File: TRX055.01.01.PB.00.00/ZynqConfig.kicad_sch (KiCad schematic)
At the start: 1 part, among them U1 XC7Z015-1CLG485I

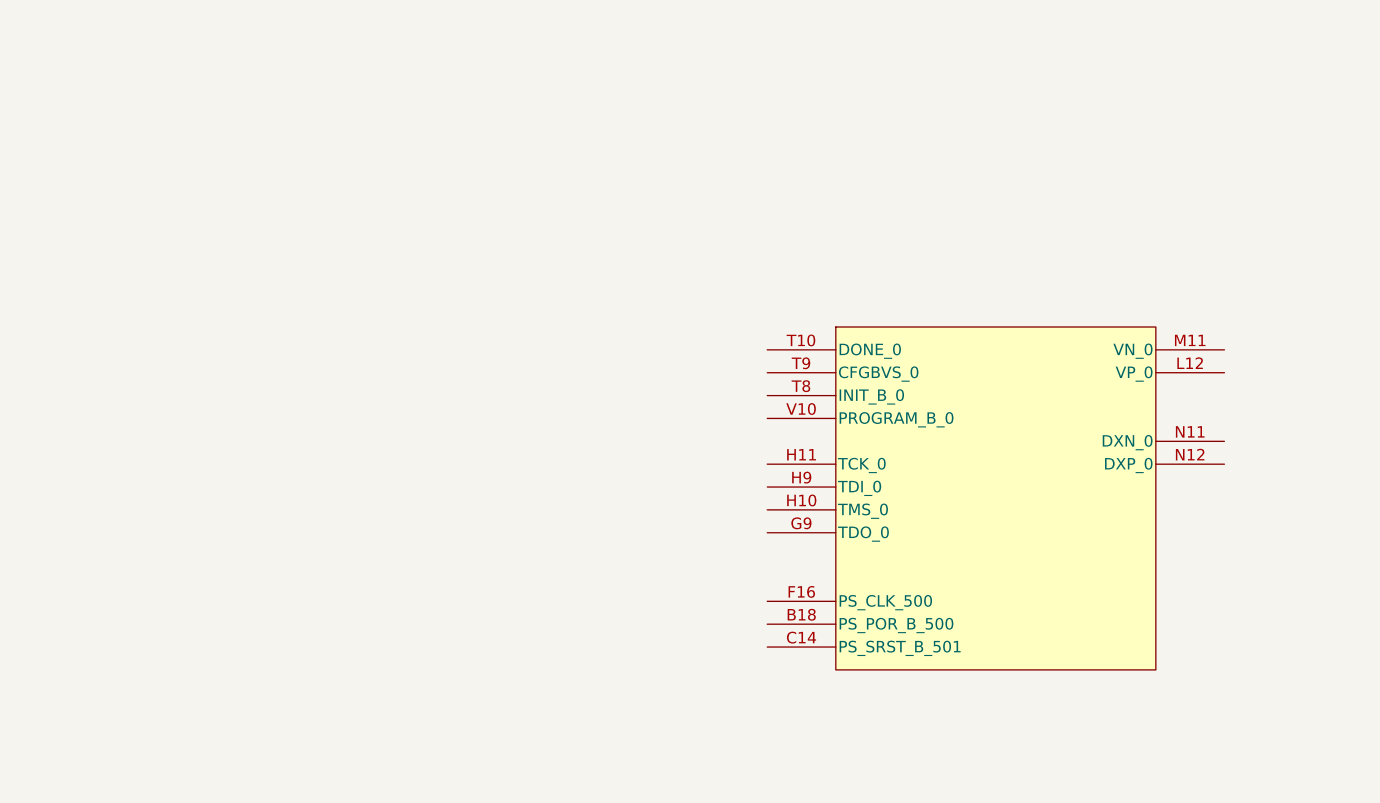
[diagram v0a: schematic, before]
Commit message: + add clocks + add PSU
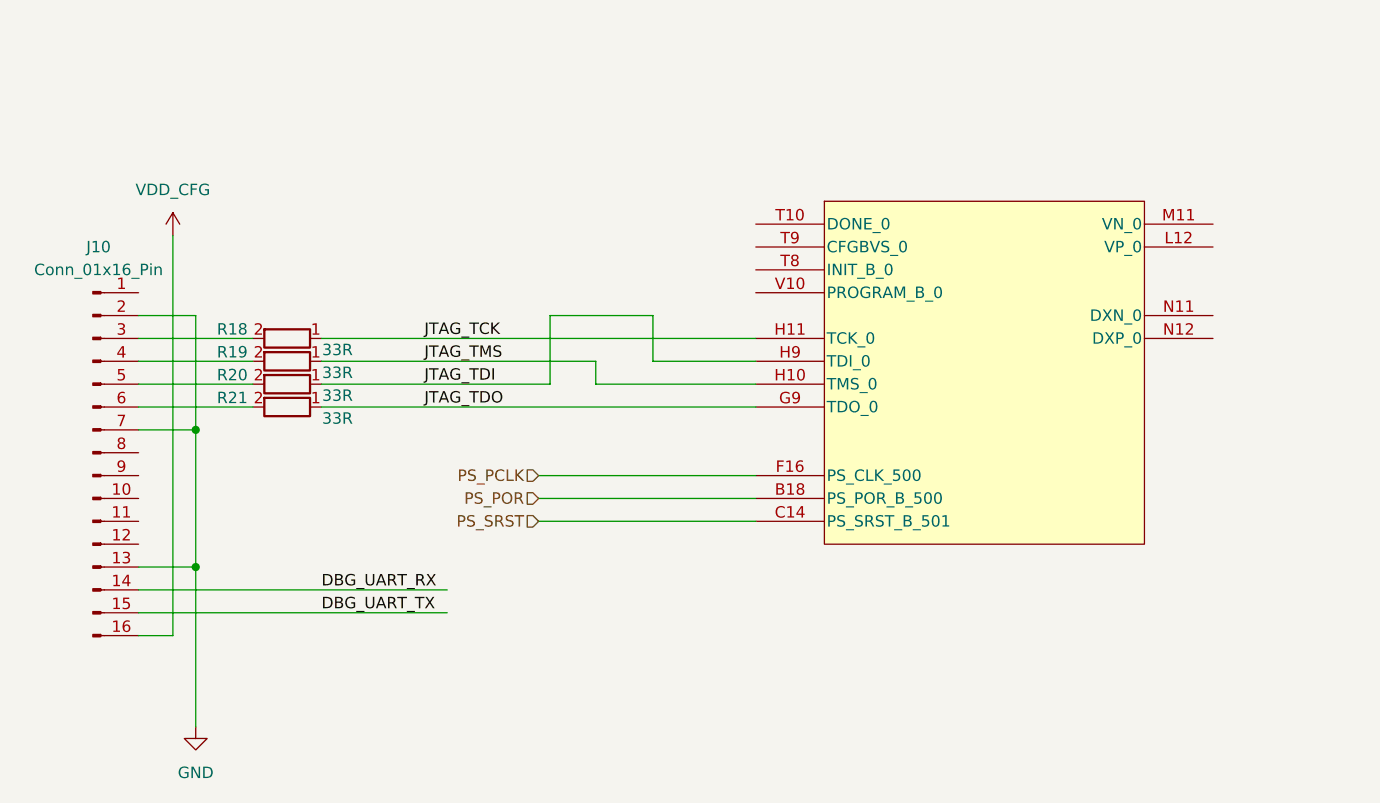
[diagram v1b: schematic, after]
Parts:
- added J10: Conn_01x16_Pin, foot-ppa-passive:FH34SRJ-16S-0.5SH, symbol Connector:Conn_01x16_Pin
- added R18, R19, R20, R21: 33R, Resistor_SMD:R_0402_1005Metric, symbol PPA-Pasive:Res
- U1: value XC7Z015-1CLG485I -> XC7Z015-2CLG485I; JLCPCB Part # C1522056 -> C1522056
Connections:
- net PS_POR: now reaches U1.B18 (PS_POR_B_500)
- net PS_SRST: now reaches U1.C14 (PS_SRST_B_501)
- net PS_PCLK: now reaches U1.F16 (PS_CLK_500)
- net JTAG_TDO: now reaches U1.G9 (TDO_0)
- net JTAG_TDO: now also R21.1
- net JTAG_TMS: now reaches U1.H10 (TMS_0)
- net JTAG_TMS: now also R19.1
- net JTAG_TCK: now reaches U1.H11 (TCK_0)
- net JTAG_TCK: now also R18.1
- net JTAG_TDI: now reaches U1.H9 (TDI_0)
- net JTAG_TDI: now also R20.1
- new net: J10.3 (Pin_3), R18.2
- new net: J10.4 (Pin_4), R19.2
- new net: J10.6 (Pin_6), R21.2
- new net: J10.5 (Pin_5), R20.2
- new net DBG_UART_RX: J10.14 (Pin_14)
- new net DBG_UART_TX: J10.15 (Pin_15)
- new net GND: J10.13 (Pin_13), J10.2 (Pin_2), J10.7 (Pin_7)
- new net VDD_CFG: J10.16 (Pin_16)

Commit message: V0.1 - production, added brig-up comments
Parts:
- added R155, R156, R159: 10K, Resistor_SMD:R_0402_1005Metric, symbol PPA-Pasive:Res
- U1: footprint CLG485XC7Z012S/XC7Z015_AMD -> XC7Z015:CLG485XC7Z012S&slash_XC7Z015_AMD
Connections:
- net GND: now also U1.T9 (CFGBVS_0), R159.1
- net PS_PCLK: now also R159.2
- net at U1.T8 (INIT_B_0): now also R156.1
- net at U1.V10 (PROGRAM_B_0): now also R155.1
- net DBG_SMU_SWDIO: now reaches J10.10 (Pin_10)
- net DBG_UART_SMU_TX: now reaches J10.11 (Pin_11)
- net DBG_UART_SMU_RX: now reaches J10.12 (Pin_12)
- net DBG_SMU_NRST: now reaches J10.8 (Pin_8)
- net DBG_SMU_SWCLK: now reaches J10.9 (Pin_9)
- net VDD_CFG renamed VCC_CFG
- net VCC_CFG: now also R155.2, R156.2
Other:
- company: (none) -> Tronex s.r.o. / Tronex Group USA LLC
- title: (none) -> TRNX SDR Carrier board
